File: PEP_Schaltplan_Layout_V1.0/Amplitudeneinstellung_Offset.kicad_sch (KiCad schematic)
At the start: 7 parts, among them U16 LT1819

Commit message: Überarbeitung und Bereinigung
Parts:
- added RV4: 10k, Potentiometer_THT:Potentiometer_Bourns_3266Y_Vertical, symbol Device:R_Potentiometer
- added SW15, SW16: SW_DIP_x04, Button_Switch_THT:SW_DIP_SPSTx04_Slide_6.7x11.72mm_W7.62mm_P2.54mm_LowProfile, symbol Switch:SW_DIP_x04
- R30: renamed from R42; value 5k -> 1k
- R31: renamed from R43; value 5k -> 1k
- RV5: renamed from RV2; value R_Potentiometer -> 10k
- renumbered R46 to R32, R47 to R33, R48 to R34, U16 to U7
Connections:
- net at R33.2, U7.1: now also RV4.2; no longer R31.1
- net at R30.2: now also SW15.5, SW16.5, SW16.6, SW16.7, SW16.8
- net +5v renamed +5V
- net -5v renamed -5V
- new net: R31.1, RV4.3
- new net Dreieck: SW16.2
- new net PWM: SW16.3
- new net Rechteck: SW16.1
- new net Sinus: SW15.4
- new net Sägezahn: SW16.4
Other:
- moved on the sheet: R30, R31, R32, R33, R34, RV5, U7A, U7B, U7C

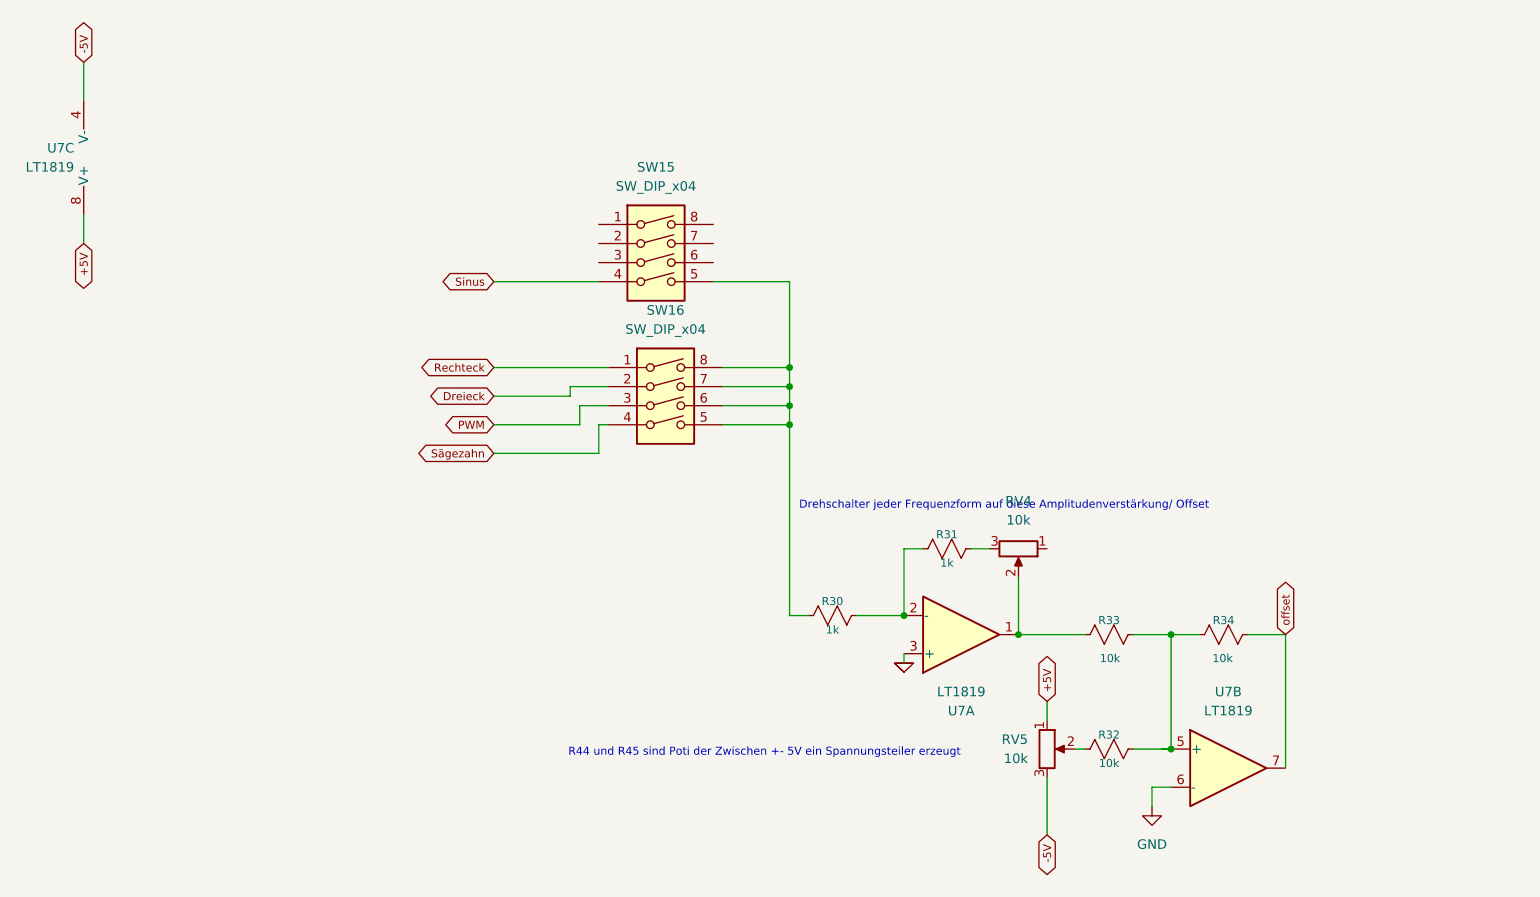
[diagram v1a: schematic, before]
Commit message: Pinheads eingefügt, GND überall (hoffentlich angebunden)
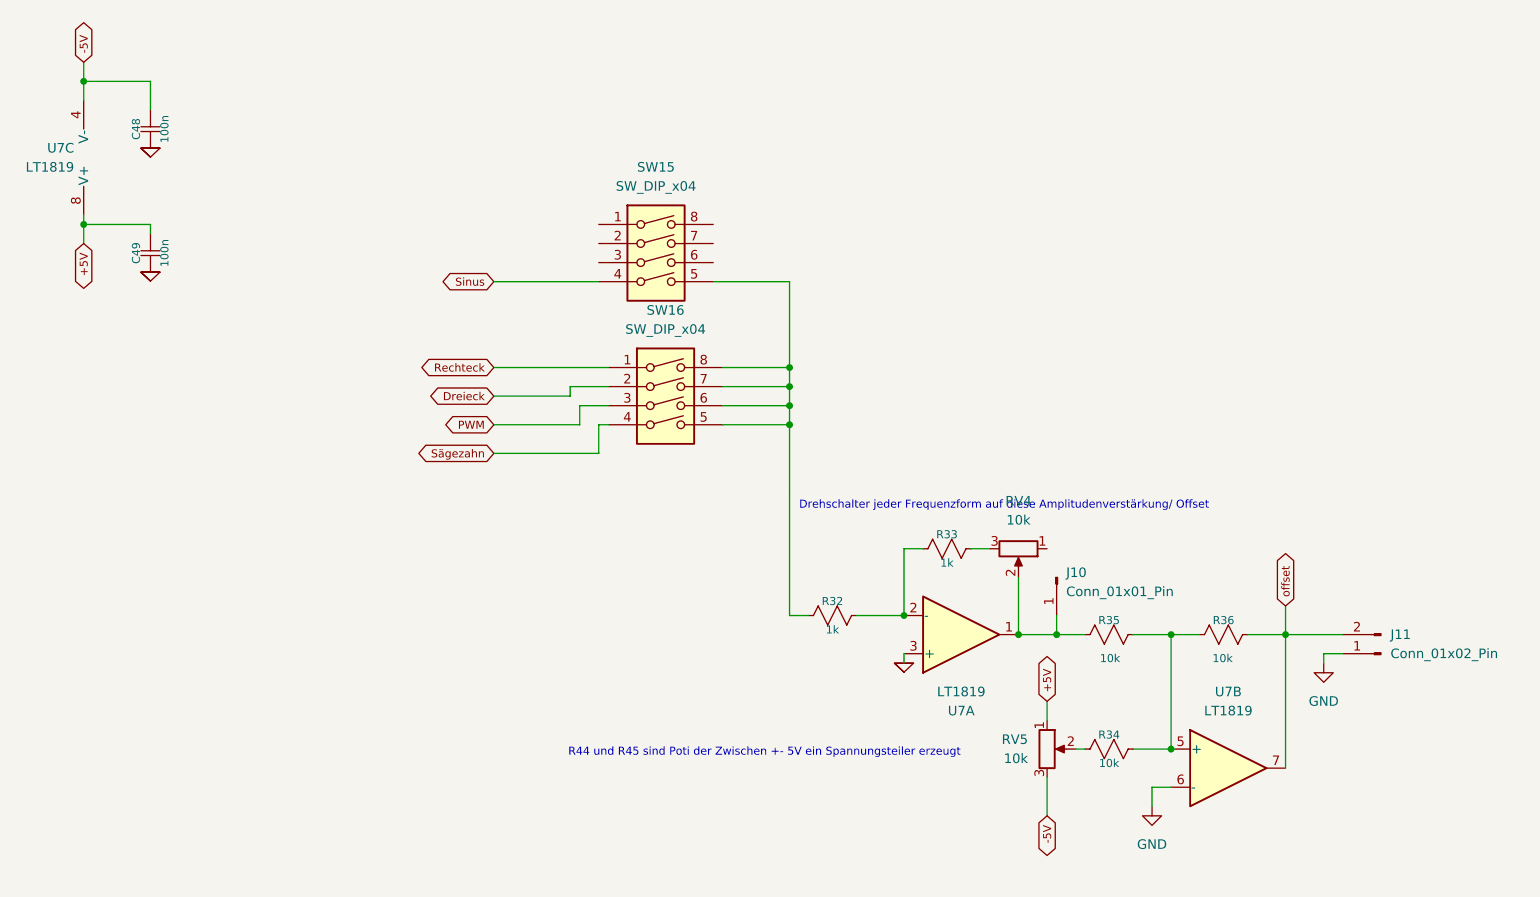
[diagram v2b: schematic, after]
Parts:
- added C48, C49: 100n, Capacitor_SMD:C_1206_3216Metric, symbol ltspice:cap
- added J10: Conn_01x01_Pin, Connector_PinSocket_2.54mm:PinSocket_1x01_P2.54mm_Vertical, symbol Connector:Conn_01x01_Pin
- added J11: Conn_01x02_Pin, Connector_PinHeader_2.54mm:PinHeader_1x02_P2.54mm_Vertical, symbol Connector:Conn_01x02_Pin
- renumbered R30 to R32, R31 to R33, R32 to R34, R33 to R35, R34 to R36
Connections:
- net +5V: now also C49.1
- net -5V: now also C48.1
- net 0: now also C48.2, C49.2
- net GND: now also J11.1 (Pin_1)
- net offset: now also J11.2 (Pin_2)
- net at R35.2, RV4.2, U7.1: now also J10.1 (Pin_1)

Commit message: Leiterplatten größe definiert und erstes Auto Routing
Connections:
- net 0 is gone; now on net GND: C48.2, C49.2, U7.3 (+)
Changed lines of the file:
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@@
 		(at 45.72 49.53 0)
 		(unit 1)
-		(body_style 0)
+		(body_style 1)
 		(exclude_from_sim no)
 		(in_bom yes)
@@
 			)
 		)
-		(property "Value" "0"
+		(property "Value" "GND"
 			(at 45.72 49.53 0)
 			(hide yes)
@@
 		(at 45.72 66.04 0)
 		(unit 1)
-		(body_style 0)
+		(body_style 1)
 		(exclude_from_sim no)
 		(in_bom yes)
@@
 			)
 		)
-		(property "Value" "0"
+		(property "Value" "GND"
 			(at 45.72 66.04 0)
 			(hide yes)
@@
 		(at 146.05 118.11 0)
 		(unit 1)
-		(body_style 0)
+		(body_style 1)
 		(exclude_from_sim no)
 		(in_bom yes)
@@
 			)
 		)
-		(property "Value" "0"
+		(property "Value" "GND"
 			(at 146.05 118.11 0)
 			(hide yes)
